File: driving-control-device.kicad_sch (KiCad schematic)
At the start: 4 parts, among them J1 Micro_SD_Card, U1 MPU-6050, U2 NEO-M9N

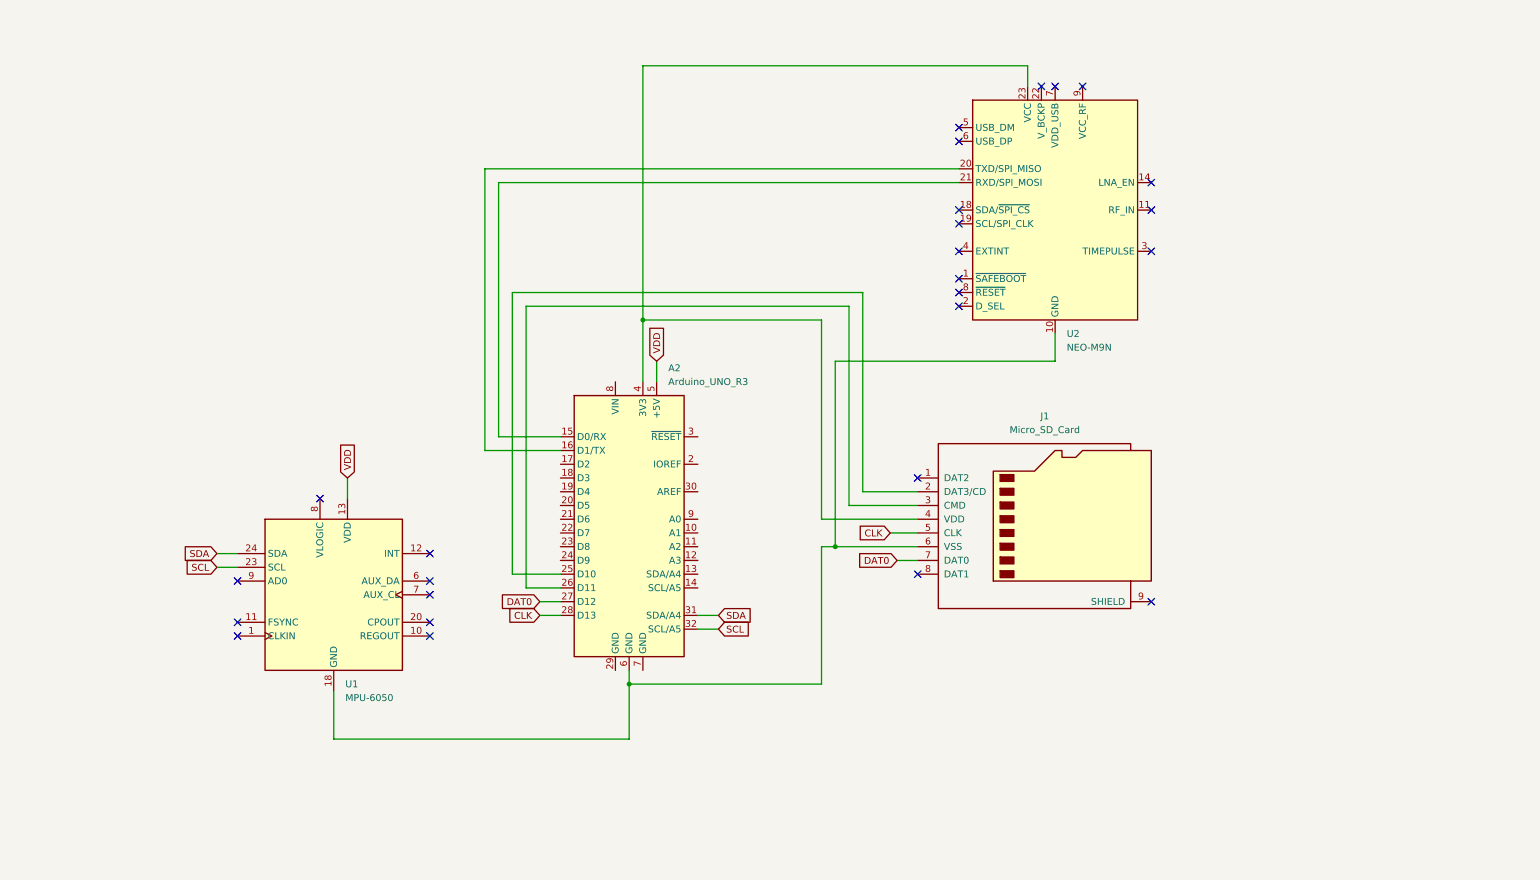
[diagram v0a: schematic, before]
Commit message: upd: principial schematic
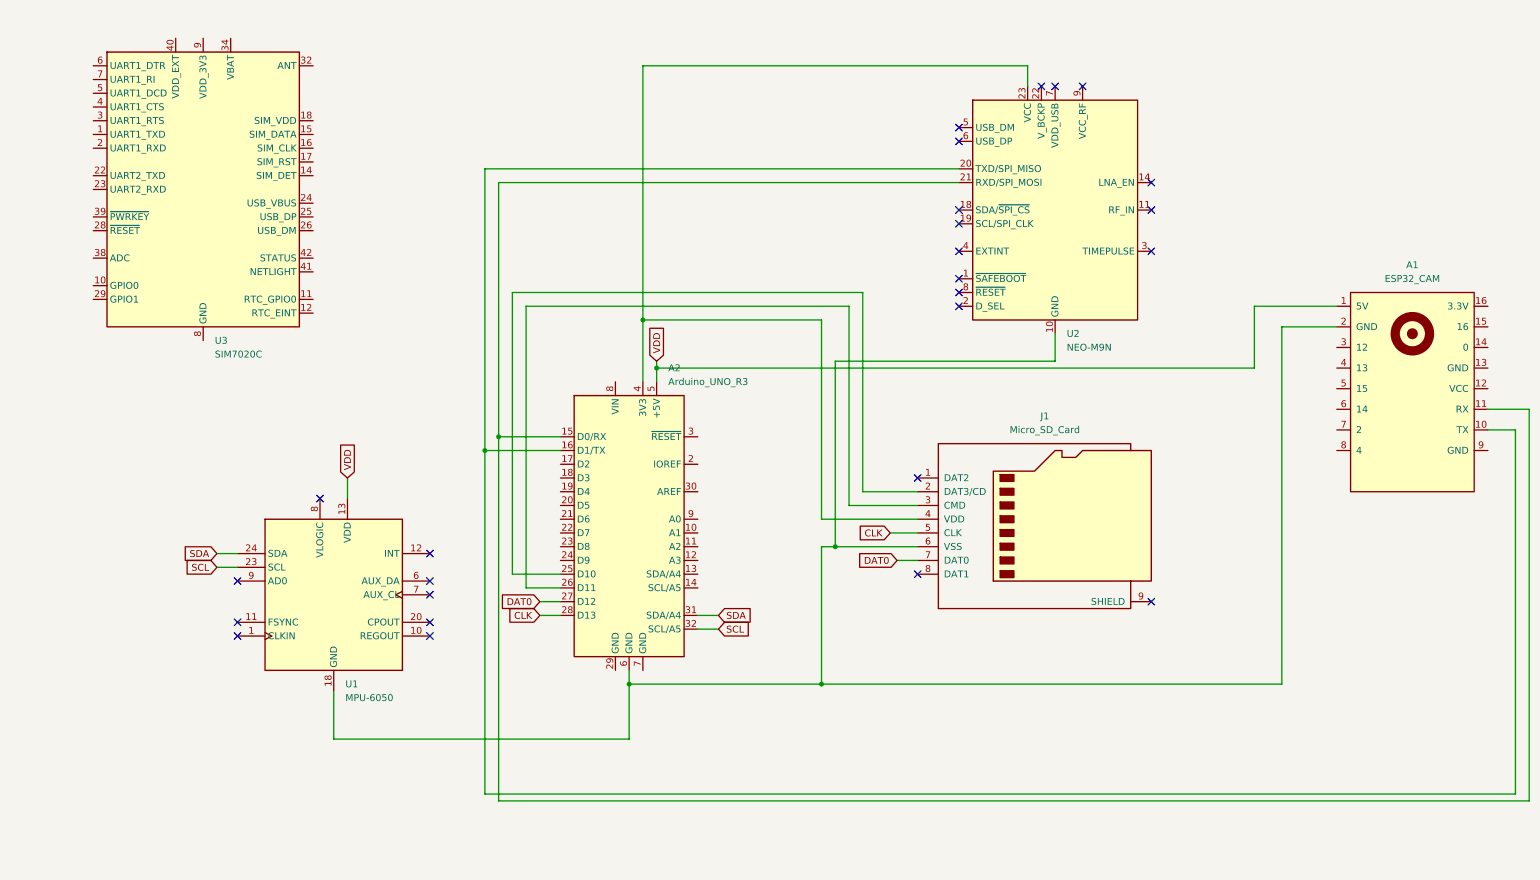
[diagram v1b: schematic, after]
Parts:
- added A1: ESP32_CAM, PCM_SL_Development_Boards:ESP32-CAM, symbol PCM_SL_Development_Board:ESP32_CAM
- added U3: SIM7020C, RF_GSM:SIMCom_SIM800C, symbol RF_GSM:SIM7020C
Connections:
- net VDD: now also A1.1 (5V)
- net at A2.6 (GND), J1.6 (VSS), U1.18 (GND)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: now also A1.2 (GND)
- net at A2.15 (D0/RX), U2.21 (RXD/SPI_MOSI): now also A1.11 (RX)
- net at A2.16 (D1/TX), U2.20 (TXD/SPI_MISO): now also A1.10 (TX)
- new net: U3.13 (GND), U3.19 (GND), U3.21 (GND), U3.27 (GND), U3.30 (GND), U3.31 (GND), U3.33 (GND), U3.36 (GND), U3.37 (GND), U3.8 (GND)
- new net: U3.34 (VBAT), U3.35 (VBAT)
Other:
- company: (none) -> РТУ МИРЭА
- title: (none) -> Устройство контроля стиля вождения

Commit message: upd: principial schematic
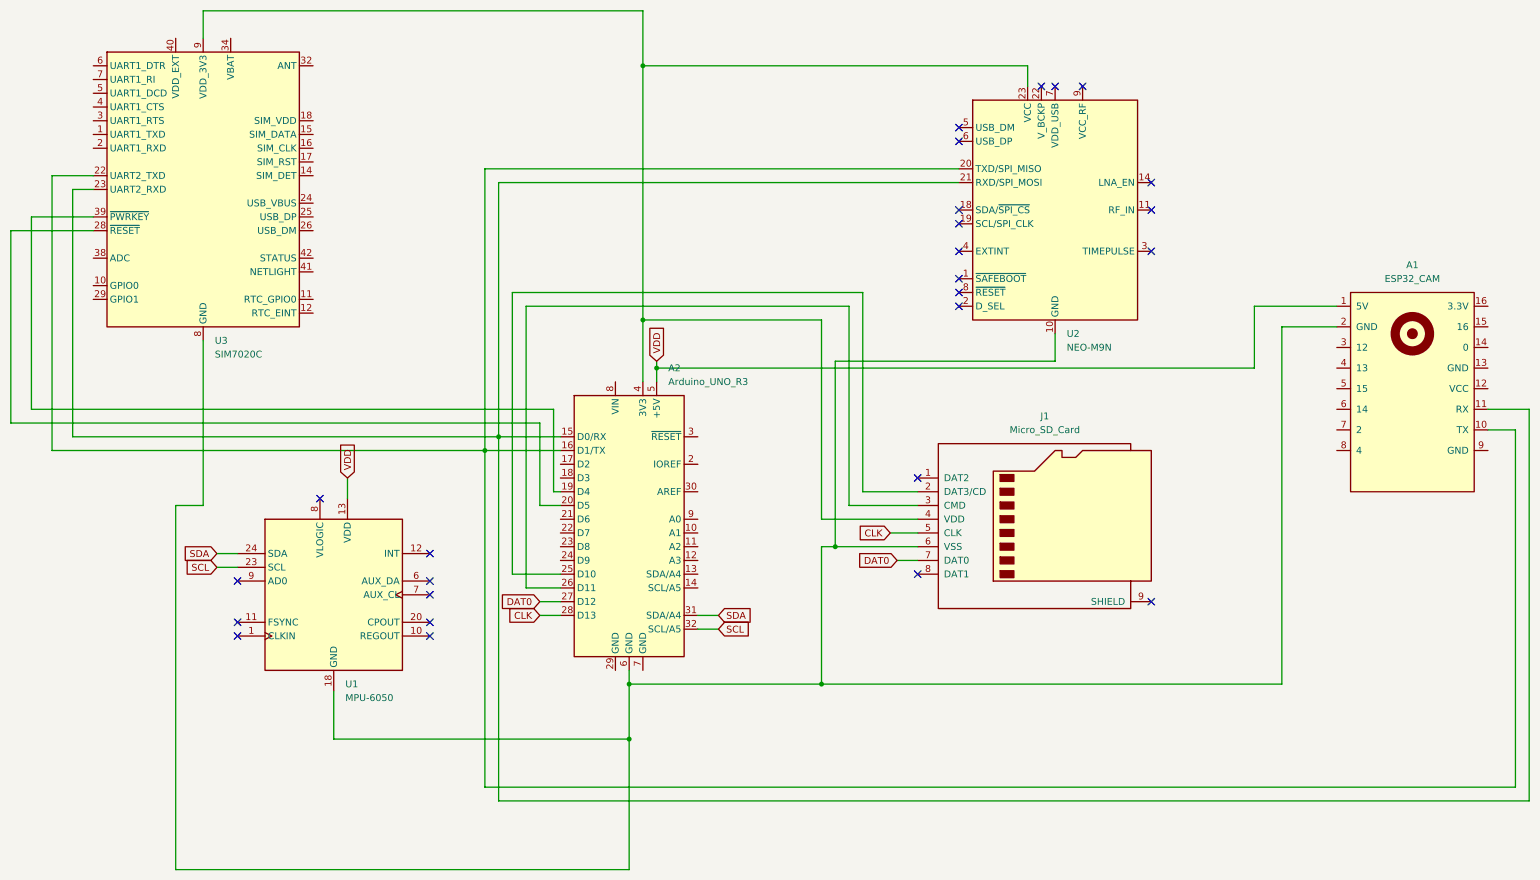
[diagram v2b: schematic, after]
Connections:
- net at U3.13 (GND), U3.19 (GND), U3.21 (GND)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: now also A1.2 (GND), A2.6 (GND), J1.6 (VSS), U1.18 (GND), U2.10 (GND), U2.12 (GND), U2.13 (GND), U2.24 (GND)
- net at U3.22 (UART2_TXD): now also A1.10 (TX), A2.16 (D1/TX), U2.20 (TXD/SPI_MISO)
- net at U3.23 (UART2_RXD): now also A1.11 (RX), A2.15 (D0/RX), U2.21 (RXD/SPI_MOSI)
- net at U3.28 (~{RESET}): now also A2.20 (D5)
- net at U3.39 (~{PWRKEY}): now also A2.19 (D4)
- net at U3.9 (VDD_3V3): now also A2.4 (3V3), J1.4 (VDD), U2.23 (VCC)
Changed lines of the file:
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@@
+	)
+	(junction
+		(at 190.5 204.47)
+		(diameter 0)
+		(color 0 0 0 0)
 	)
 	(junction
@@
 	)
 	(junction
+		(at 193.04 80.01)
+		(diameter 0)
+		(color 0 0 0 0)
+	)
+	(junction
 		(at 195.58 135.89)
 		(diameter 0)
@@
 	(wire
 		(pts
+			(xy 91.44 102.87) (xy 87.63 102.87)
+		)
+		(stroke
+			(width 0)
+			(type default)
+		)
+	)
+	(wire
+		(pts
 			(xy 264.16 80.01) (xy 264.16 83.82)
 		)
@@
 	(wire
 		(pts
+			(xy 173.99 161.29) (xy 177.8 161.29)
+		)
+		(stroke
+			(width 0)
+			(type default)
+		)
+	)
+	(wire
+		(pts
 			(xy 269.24 129.54) (xy 269.24 134.62)
 		)
@@
 	(wire
 		(pts
+			(xy 87.63 102.87) (xy 87.63 148.59)
+		)
+		(stroke
+			(width 0)
+			(type default)
+		)
+	)
+	(wire
+		(pts
 			(xy 195.58 135.89) (xy 195.58 138.43)
 		)
@@
 	(wire
 		(pts
+			(xy 111.76 69.85) (xy 193.04 69.85)
+		)
+		(stroke
+			(width 0)
+			(type default)
+		)
+	)
+	(wire
+		(pts
 			(xy 138.43 156.21) (xy 138.43 160.02)
 		)
@@
 	(wire
 		(pts
+			(xy 176.53 158.75) (xy 177.8 158.75)
+		)
+		(stroke
+			(width 0)
+			(type default)
+		)
+	)
+	(wire
+		(pts
 			(xy 166.37 215.9) (xy 356.87 215.9)
 		)
@@
 	(wire
 		(pts
+			(xy 173.99 146.05) (xy 173.99 161.29)
+		)
+		(stroke
+			(width 0)
+			(type default)
+		)
+	)
+	(wire
+		(pts
 			(xy 233.68 158.75) (xy 233.68 121.92)
 		)
@@
 	(wire
 		(pts
-			(xy 354.33 214.63) (xy 163.83 214.63)
+			(xy 354.33 213.36) (xy 163.83 213.36)
+		)
+		(stroke
+			(width 0)
+			(type default)
+		)
+	)
+	(wire
+		(pts
+			(xy 83.82 100.33) (xy 83.82 151.13)
 		)
 		(stroke
@@
 	(wire
 		(pts
+			(xy 106.68 161.29) (xy 106.68 228.6)
+		)
+		(stroke
+			(width 0)
+			(type default)
+		)
+	)
+	(wire
+		(pts
 			(xy 114.3 172.72) (xy 118.11 172.72)
 		)
@@
 	(wire
 		(pts
+			(xy 83.82 151.13) (xy 163.83 151.13)
+		)
+		(stroke
+			(width 0)
+			(type default)
+		)
+	)
+	(wire
+		(pts
 			(xy 251.46 99.06) (xy 163.83 99.06)
 		)
@@
 	(wire
 		(pts
+			(xy 76.2 110.49) (xy 76.2 146.05)
+		)
+		(stroke
+			(width 0)
+			(type default)
+		)
+	)
+	(wire
+		(pts
+			(xy 80.01 107.95) (xy 80.01 143.51)
+		)
+		(stroke
+			(width 0)
+			(type default)
+		)
+	)
+	(wire
+		(pts
 			(xy 228.6 168.91) (xy 226.06 168.91)
 		)
@@
 	(wire
 		(pts
+			(xy 91.44 107.95) (xy 80.01 107.95)
+		)
+		(stroke
+			(width 0)
+			(type default)
+		)
+	)
+	(wire
+		(pts
 			(xy 264.16 80.01) (xy 193.04 80.01)
 		)
@@
 	(wire
 		(pts
+			(xy 190.5 228.6) (xy 190.5 204.47)
+		)
+		(stroke
+			(width 0)
+			(type default)
+		)
+	)
+	(wire
+		(pts
 			(xy 228.6 134.62) (xy 228.6 168.91)
 		)
@@
 	(wire
 		(pts
+			(xy 91.44 110.49) (xy 76.2 110.49)
+		)
+		(stroke
+			(width 0)
+			(type default)
+		)
+	)
+	(wire
+		(pts
+			(xy 76.2 146.05) (xy 173.99 146.05)
+		)
+		(stroke
+			(width 0)
+			(type default)
+		)
+	)
+	(wire
+		(pts
+			(xy 111.76 130.81) (xy 111.76 161.29)
+		)
+		(stroke
+			(width 0)
+			(type default)
+		)
+	)
+	(wire
+		(pts
 			(xy 171.45 176.53) (xy 177.8 176.53)
 		)
@@
 	(wire
 		(pts
-			(xy 163.83 151.13) (xy 163.83 214.63)
+			(xy 163.83 151.13) (xy 163.83 213.36)
+		)
+		(stroke
+			(width 0)
+			(type default)
+		)
+	)
+	(wire
+		(pts
+			(xy 80.01 143.51) (xy 176.53 143.51)
 		)
 		(stroke
@@
 	(wire
 		(pts
+			(xy 111.76 161.29) (xy 106.68 161.29)
+		)
+		(stroke
+			(width 0)
+			(type default)
+		)
+	)
+	(wire
+		(pts
 			(xy 226.06 163.83) (xy 226.06 127)
 		)
@@
 	(wire
 		(pts
+			(xy 111.76 69.85) (xy 111.76 74.93)
+		)
+		(stroke
+			(width 0)
+			(type default)
+		)
+	)
+	(wire
+		(pts
+			(xy 91.44 100.33) (xy 83.82 100.33)
+		)
+		(stroke
+			(width 0)
+			(type default)
+		)
+	)
+	(wire
+		(pts
 			(xy 171.45 124.46) (xy 171.45 176.53)
 		)
@@
 	(wire
 		(pts
+			(xy 193.04 69.85) (xy 193.04 80.01)
+		)
+		(stroke
+			(width 0)
+			(type default)
+		)
+	)
+	(wire
+		(pts
 			(xy 311.15 194.31) (xy 226.06 194.31)
 		)
@@
 	(wire
 		(pts
+			(xy 106.68 228.6) (xy 190.5 228.6)
+		)
+		(stroke
+			(width 0)
+			(type default)
+		)
+	)
+	(wire
+		(pts
 			(xy 243.84 168.91) (xy 228.6 168.91)
 		)
@@
 	(wire
 		(pts
-			(xy 354.33 147.32) (xy 354.33 214.63)
+			(xy 354.33 147.32) (xy 354.33 213.36)
 		)
 		(stroke
@@
 	(wire
 		(pts
+			(xy 176.53 143.51) (xy 176.53 158.75)
+		)
+		(stroke
+			(width 0)
+			(type default)
+		)
+	)
+	(wire
+		(pts
 			(xy 135.89 204.47) (xy 190.5 204.47)
 		)
 		(stroke
+			(width 0)
+			(type default)
+		)
+	)
+	(wire
+		(pts
+			(xy 87.63 148.59) (xy 166.37 148.59)
+		)
+		(stroke
